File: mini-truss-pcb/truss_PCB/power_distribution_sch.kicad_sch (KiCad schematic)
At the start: 38 parts, among them IC1 BAJ0BC0FP-E2, J16 GND, J17 GND, J18 12V, J19 6V, J20 5V_MCU, J21 3V3, J22 10V, Q8 IRF5305_PBF, U11 LM2596S-ADJ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

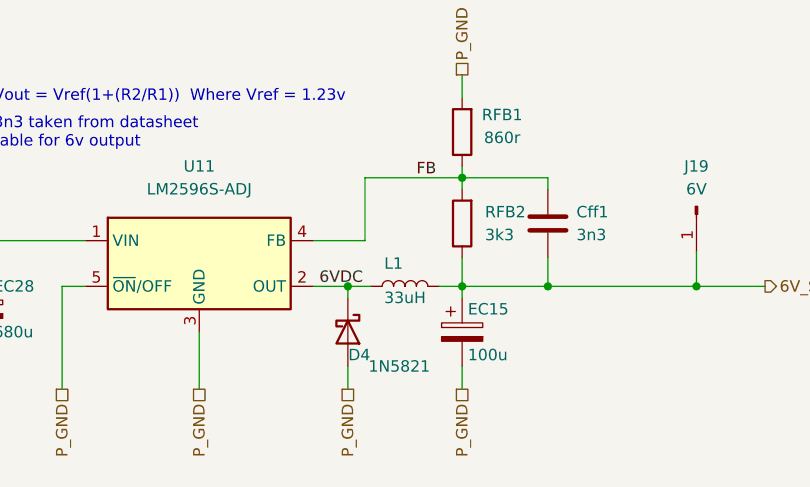
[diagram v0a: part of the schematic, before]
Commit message: added basic firmware tests
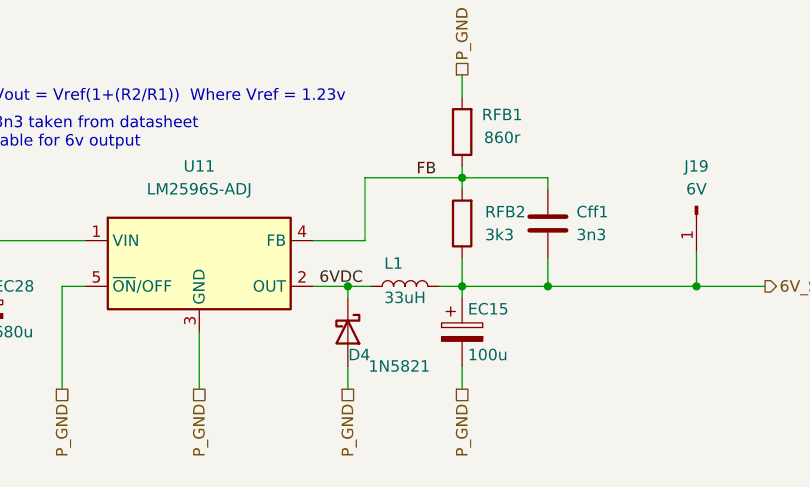
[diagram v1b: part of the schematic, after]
